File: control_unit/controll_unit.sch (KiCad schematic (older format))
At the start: 22 parts, among them J1 Screw_Terminal_1x02, J2 Screw_Terminal_1x04, P1 USB_A, P2 CONN_01X20, Q1 Q_NPN_BCE, Q2 Q_NPN_BCE, Q3 Q_NPN_BCE, U1 LM2576HV, U2 push_button, U3 push_button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

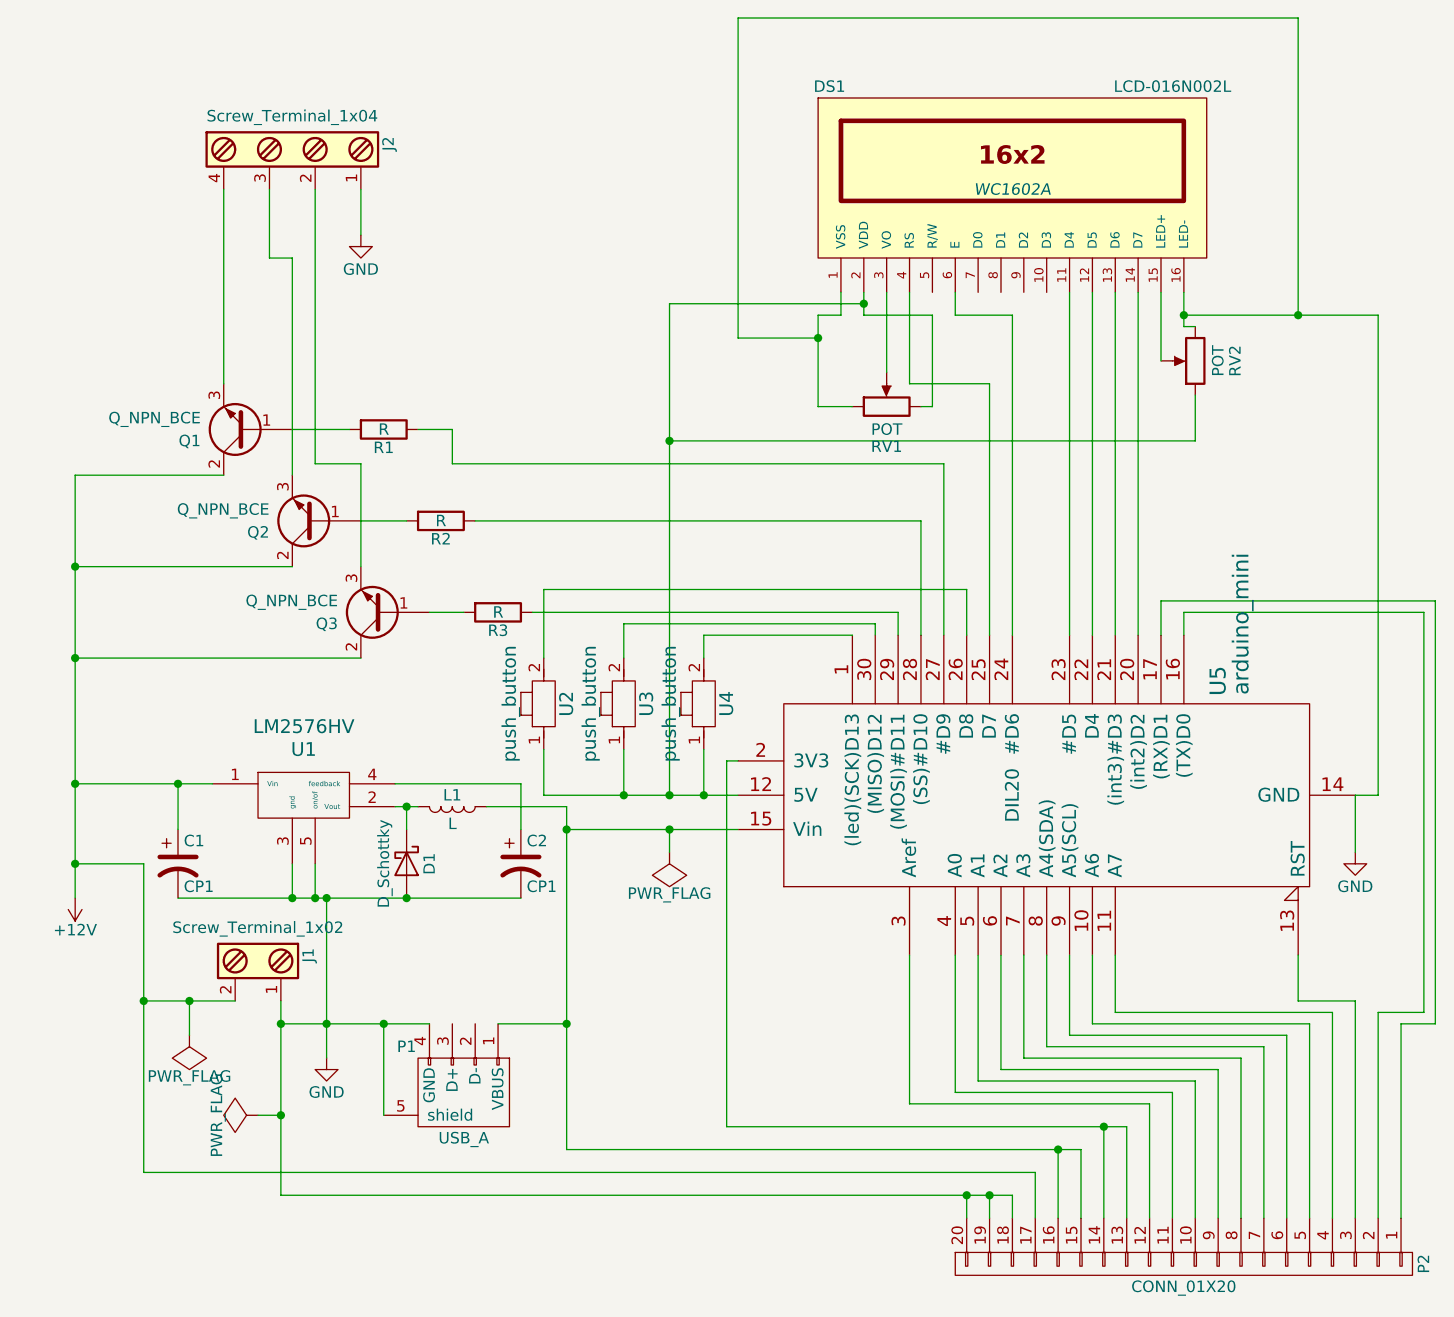
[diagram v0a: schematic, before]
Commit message: Single transistor amp pabeigs komponensu layout
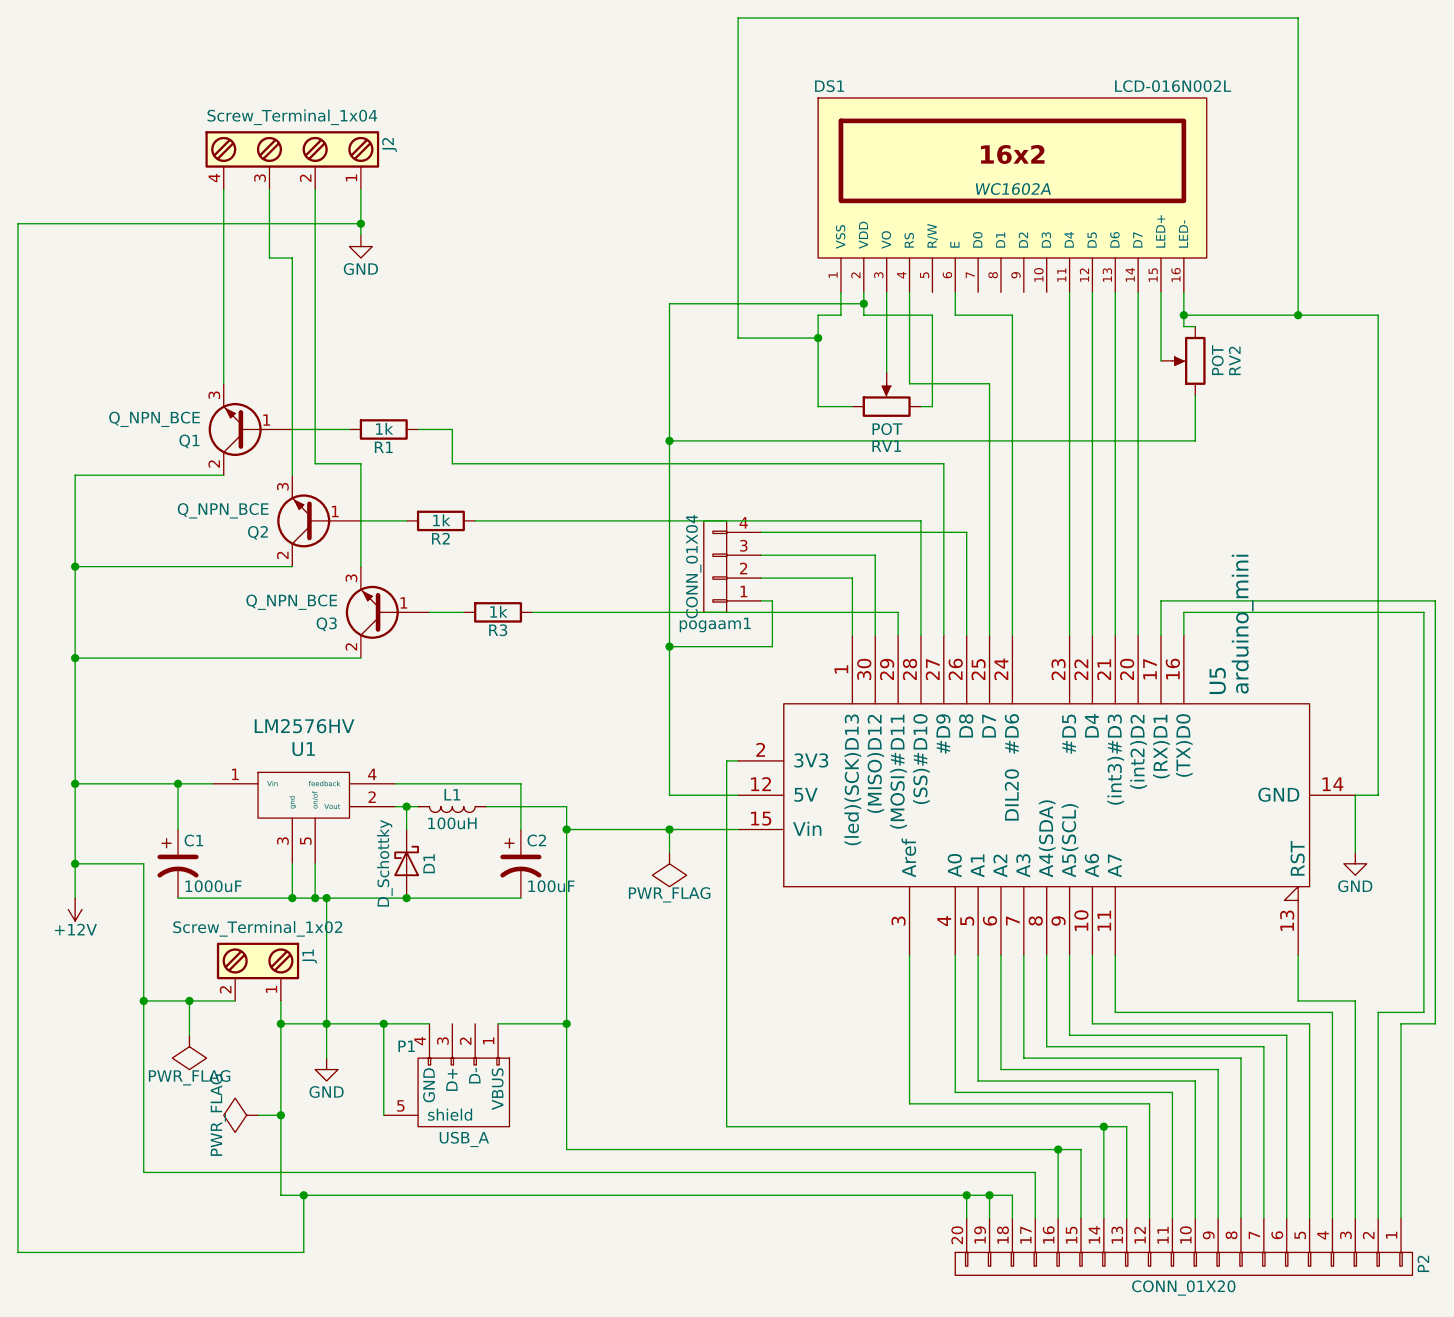
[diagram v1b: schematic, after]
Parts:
- removed U2, U3, U4: push_button, symbol push_button
- added pogaam1: CONN_01X04, Connectors:bornier4, symbol CONN_01X04
- C1: value CP1 -> 1000uF; footprint (none) -> Capacitors_THT:CP_Radial_D12.5mm_P5.00mm
- C2: value CP1 -> 100uF; footprint (none) -> Capacitors_THT:CP_Radial_D5.0mm_P2.00mm
- D1: footprint (none) -> Diodes_THT:D_DO-41_SOD81_P10.16mm_Horizontal
- J1: footprint (none) -> Connectors_Terminal_Blocks:TerminalBlock_Pheonix_PT-3.5mm_2pol
- J2: footprint (none) -> Connectors_Terminal_Blocks:TerminalBlock_Pheonix_PT-3.5mm_4pol
- L1: value L -> 100uH
- P1: footprint (none) -> Connectors:USB_A
- P2: footprint (none) -> Connectors:IDC_Header_Straight_20pins
- Q1, Q2, Q3: footprint (none) -> TO_SOT_Packages_THT:TO-220_Vertical
- R1, R2, R3: value R -> 1k; footprint (none) -> Resistors_THT:R_Axial_DIN0617_L17.0mm_D6.0mm_P25.40mm_Horizontal
- RV1, RV2: footprint (none) -> Potentiometers:Potentiometer_Trimmer_Piher_PT-10v5_Horizontal_Px5.0mm_Py5.0mm
- U1: footprint (none) -> TO_SOT_Packages_THT:TO-220-5_Pentawatt_Multiwatt-5_Vertical
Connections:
- net at DS1.2 (VDD), RV1.3, RV2.1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: now also pogaam1.1 (P1)
- net at U5.1 ((led)(SCK)D13): now also pogaam1.2 (P2)
- net at U5.26 (D8): now also pogaam1.4 (P4)
- net at U5.30 ((MISO)D12): now also pogaam1.3 (P3)
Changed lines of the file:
@@
 F 1 "LCD-016N002L" H 5850 3150 50  0000 C CNN
 F 2 "WC1602A" H 5150 2700 50  0000 C CIN
-F 3 "" H 5150 2750 50  0000 C CNN
+F 3 "https://www.openhacks.com/uploadsproductos/eone-1602a1.pdf" H 5150 2750 50  0001 C CNN
 	1    5150 2750
 	1    0    0    -1
@@
 F 1 "arduino_mini" H 5850 4400 70  0000 C CNN
 F 2 "DIL20" H 5100 5400 60  0000 C CNN
-F 3 "" H 5100 5450 60  0001 C CNN
+F 3 "https://www.arduino.cc/en/uploads/Main/ArduinoNanoManual23.pdf" H 5100 5450 60  0001 C CNN
 	1    5100 5450
 	0    -1   -1   0
@@
 F 0 "RV1" V 4425 3750 50  0000 C CNN
 F 1 "POT" V 4500 3750 50  0000 C CNN
-F 2 "" H 4600 3750 50  0000 C CNN
-F 3 "" H 4600 3750 50  0000 C CNN
+F 2 "Potentiometers:Potentiometer_Trimmer_Piher_PT-10v5_Horizontal_Px5.0mm_Py5.0mm" H 4600 3750 50  0001 C CNN
+F 3 "http://www.dipmicro.com/?datasheet=RM065.pdf" H 4600 3750 50  0001 C CNN
 	1    4600 3750
 	0    -1   -1   0
@@
 F 0 "RV2" V 5775 3550 50  0000 C CNN
 F 1 "POT" V 5850 3550 50  0000 C CNN
-F 2 "" H 5950 3550 50  0000 C CNN
-F 3 "" H 5950 3550 50  0000 C CNN
+F 2 "Potentiometers:Potentiometer_Trimmer_Piher_PT-10v5_Horizontal_Px5.0mm_Py5.0mm" H 5950 3550 50  0001 C CNN
+F 3 "http://www.dipmicro.com/?datasheet=RM065.pdf" H 5950 3550 50  0001 C CNN
 	1    5950 3550
 	-1   0    0    1
@@
 F 0 "Q3" H 2600 4700 50  0000 L CNN
 F 1 "Q_NPN_BCE" H 2600 4600 50  0000 L CNN
-F 2 "" H 2600 4750 50  0000 C CNN
-F 3 "" H 2400 4650 50  0000 C CNN
+F 2 "TO_SOT_Packages_THT:TO-220_Vertical" H 2600 4750 50  0001 C CNN
+F 3 "http://www.hobbytronics.co.uk/datasheets/TIP31.pdf" H 2400 4650 50  0001 C CNN
 	1    2400 4650
 	-1   0    0    1
@@
 F 0 "Q2" H 2300 4300 50  0000 L CNN
 F 1 "Q_NPN_BCE" H 2300 4200 50  0000 L CNN
-F 2 "" H 2300 4350 50  0000 C CNN
-F 3 "" H 2100 4250 50  0000 C CNN
+F 2 "TO_SOT_Packages_THT:TO-220_Vertical" H 2300 4350 50  0001 C CNN
+F 3 "http://www.hobbytronics.co.uk/datasheets/TIP31.pdf" H 2100 4250 50  0001 C CNN
 	1    2100 4250
 	-1   0    0    1
@@
 F 0 "Q1" H 2000 3900 50  0000 L CNN
 F 1 "Q_NPN_BCE" H 2000 3800 50  0000 L CNN
-F 2 "" H 2000 3950 50  0000 C CNN
-F 3 "" H 1800 3850 50  0000 C CNN
+F 2 "TO_SOT_Packages_THT:TO-220_Vertical" H 2000 3950 50  0001 C CNN
+F 3 "http://www.hobbytronics.co.uk/datasheets/TIP31.pdf" H 1800 3850 50  0001 C CNN
 	1    1800 3850
 	-1   0    0    1
@@
 P 2400 3850
 F 0 "R1" V 2480 3850 50  0000 C CNN
-F 1 "R" V 2400 3850 50  0000 C CNN
-F 2 "" V 2330 3850 50  0000 C CNN
-F 3 "" H 2400 3850 50  0000 C CNN
+F 1 "1k" V 2400 3850 50  0000 C CNN
+F 2 "Resistors_THT:R_Axial_DIN0617_L17.0mm_D6.0mm_P25.40mm_Horizontal" H 2330 3850 50  0001 C CNN
+F 3 "https://lib.chipdip.ru/505/DOC001505920.pdf" H 2400 3850 50  0001 C CNN
 	1    2400 3850
 	0    1    1    0
@@
 P 2650 4250
 F 0 "R2" V 2730 4250 50  0000 C CNN
-F 1 "R" V 2650 4250 50  0000 C CNN
-F 2 "" V 2580 4250 50  0000 C CNN
-F 3 "" H 2650 4250 50  0000 C CNN
+F 1 "1k" V 2650 4250 50  0000 C CNN
+F 2 "Resistors_THT:R_Axial_DIN0617_L17.0mm_D6.0mm_P25.40mm_Horizontal" H 2580 4250 50  0001 C CNN
+F 3 "https://lib.chipdip.ru/505/DOC001505920.pdf" H 2650 4250 50  0001 C CNN
 	1    2650 4250
 	0    1    1    0
@@
 P 2900 4650
 F 0 "R3" V 2980 4650 50  0000 C CNN
-F 1 "R" V 2900 4650 50  0000 C CNN
-F 2 "" V 2830 4650 50  0000 C CNN
-F 3 "" H 2900 4650 50  0000 C CNN
+F 1 "1k" V 2900 4650 50  0000 C CNN
+F 2 "Resistors_THT:R_Axial_DIN0617_L17.0mm_D6.0mm_P25.40mm_Horizontal" V 2830 4650 50  0001 C CNN
+F 3 "https://lib.chipdip.ru/505/DOC001505920.pdf" H 2900 4650 50  0001 C CNN
 	1    2900 4650
 	0    1    1    0
@@
 F 0 "J2" H 2000 3050 50  0000 C TNN
 F 1 "Screw_Terminal_1x04" V 1850 2600 50  0000 C TNN
-F 2 "" H 2000 2175 50  0001 C CNN
-F 3 "" H 1975 2800 50  0001 C CNN
+F 2 "Connectors_Terminal_Blocks:TerminalBlock_Pheonix_PT-3.5mm_4pol" H 2000 2175 50  0001 C CNN
+F 3 "http://www.altechcorp.com/PDFS/PCB-Pluggable.pdf" H 1975 2800 50  0001 C CNN
 	1    2000 2600
 	0    1    1    0
@@
 F 0 "P2" H 5900 8550 50  0000 C CNN
 F 1 "CONN_01X20" V 6000 7500 50  0000 C CNN
-F 2 "" H 5900 7500 50  0000 C CNN
-F 3 "" H 5900 7500 50  0000 C CNN
+F 2 "Connectors:IDC_Header_Straight_20pins" H 5900 7500 50  0001 C CNN
+F 3 "http://www.mmtmachrone.com/pdf/20090217224253PHa.pdf" H 5900 7500 50  0001 C CNN
 	1    5900 7500
 	0    1    1    0
@@
 F 0 "P1" H 2900 6550 50  0000 C CNN
 F 1 "USB_A" H 2650 6950 50  0000 C CNN
-F 2 "" V 2650 6650 50  0000 C CNN
-F 3 "" V 2650 6650 50  0000 C CNN
+F 2 "Connectors:USB_A" V 2650 6650 50  0001 C CNN
+F 3 "http://www.te.com/commerce/DocumentDelivery/DDEController?Action=showdoc&DocId=Data+Sheet%7F7-1773442-0%7F0306%7Fpdf%7FEnglish%7FENG_DS_7-1773442-0_0306.pdf%7F292336-1" H 2650 6650 50  0001 C CNN
 	1    2700 6750
 	-1   0    0    1
@@
 F 0 "U1" H 2050 5650 60  0000 C CNN
 F 1 "LM2576HV" H 2050 5750 60  0000 C CNN
-F 2 "" H 2100 5450 60  0001 C CNN
-F 3 "" H 2100 5450 60  0001 C CNN
+F 2 "TO_SOT_Packages_THT:TO-220-5_Pentawatt_Multiwatt-5_Vertical" H 2100 5450 60  0001 C CNN
+F 3 "http://www.ti.com/lit/ds/symlink/lm2576.pdf" H 2100 5450 60  0001 C CNN
 	1    2050 5450
 	1    0    0    -1
@@
 P 1500 5750
 F 0 "C1" H 1525 5850 50  0000 L CNN
-F 1 "CP1" H 1525 5650 50  0000 L CNN
-F 2 "" H 1500 5750 50  0000 C CNN
-F 3 "" H 1500 5750 50  0000 C CNN
+F 1 "1000uF" H 1525 5650 50  0000 L CNN
+F 2 "Capacitors_THT:CP_Radial_D12.5mm_P5.00mm" H 1500 5750 50  0001 C CNN
+F 3 "http://www.yageo.com/exep/pages/download/literatures/E-cap_2011.pdf" H 1500 5750 50  0001 C CNN
 	1    1500 5750
 	1    0    0    -1
@@
 F 0 "D1" H 2500 5850 50  0000 C CNN
 F 1 "D_Schottky" H 2500 5650 50  0000 C CNN
-F 2 "" H 2500 5750 50  0000 C CNN
-F 3 "" H 2500 5750 50  0000 C CNN
+F 2 "Diodes_THT:D_DO-41_SOD81_P10.16mm_Horizontal" H 2500 5750 50  0001 C CNN
+F 3 "https://www.pdp8online.com/mfm/board/datasheets/Fairchild_1N5820.pdf" H 2500 5750 50  0001 C CNN
 	1    2500 5750
 	0    1    1    0
@@
 P 2700 5500
 F 0 "L1" V 2650 5500 50  0000 C CNN
-F 1 "L" V 2775 5500 50  0000 C CNN
+F 1 "100uH" V 2775 5500 50  0000 C CNN
 F 2 "" H 2700 5500 50  0000 C CNN
-F 3 "" H 2700 5500 50  0000 C CNN
+F 3 "https://www.ineltro.ch/media/downloads/SAAItem/25/25670/564c7d97-85b8-461e-a4cf-90b6538cd451.pdf" H 2700 5500 50  0001 C CNN
 	1    2700 5500
 	0    1    1    0
@@
 P 3000 5750
 F 0 "C2" H 3025 5850 50  0000 L CNN
-F 1 "CP1" H 3025 5650 50  0000 L CNN
-F 2 "" H 3000 5750 50  0000 C CNN
-F 3 "" H 3000 5750 50  0000 C CNN
+F 1 "100uF" H 3025 5650 50  0000 L CNN
+F 2 "Capacitors_THT:CP_Radial_D5.0mm_P2.00mm" H 3000 5750 50  0001 C CNN
+F 3 "https://www.arduino.cc/documents/datasheets/cap100uF.pdf" H 3000 5750 50  0001 C CNN
 	1    3000 5750
 	1    0    0    -1
-$EndComp
-$Comp
-L push_button U2
-U 1 1 59121AF8
-P 3100 5050
-F 0 "U2" H 3100 4950 60  0000 C CNN
-F 1 "push_button" H 3100 5200 60  0000 C CNN
-F 2 "" H 3100 5050 60  0001 C CNN
-F 3 "" H 3100 5050 60  0001 C CNN
-	1    3100 5050
-	0    -1   -1   0
-$EndComp
-$Comp
-L push_button U3
-U 1 1 59121BAB
-P 3450 5050
-F 0 "U3" H 3450 4950 60  0000 C CNN
-F 1 "push_button" H 3450 5200 60  0000 C CNN
-F 2 "" H 3450 5050 60  0001 C CNN
-F 3 "" H 3450 5050 60  0001 C CNN
-	1    3450 5050
-	0    -1   -1   0
-$EndComp
-$Comp
-L push_button U4
-U 1 1 59121DF6
-P 3800 5050
-F 0 "U4" H 3800 4950 60  0000 C CNN
-F 1 "push_button" H 3800 5200 60  0000 C CNN
-F 2 "" H 3800 5050 60  0001 C CNN
-F 3 "" H 3800 5050 60  0001 C CNN
-	1    3800 5050
-	0    -1   -1   0
 $EndComp
 $Comp
@@
 F 0 "J1" H 1850 6400 50  0000 C TNN
 F 1 "Screw_Terminal_1x02" V 1700 6150 50  0000 C TNN
-F 2 "" H 1850 5925 50  0001 C CNN
-F 3 "" H 1825 6150 50  0001 C CNN
+F 2 "Connectors_Terminal_Blocks:TerminalBlock_Pheonix_PT-3.5mm_2pol" H 1850 5925 50  0001 C CNN
+F 3 "http://www.altechcorp.com/PDFS/PCB-Pluggable.pdf" H 1825 6150 50  0001 C CNN
 	1    1850 6150
 	0    1    1    0
@@
 	5050 3650 5050 4750
 Wire Wire Line
-	3100 5450 3950 5450
-Wire Wire Line
 	4500 3250 4500 3350
 Wire Wire Line
@@
 	3200 5600 3950 5600
 Wire Wire Line
-	4950 4750 4950 4550
-Wire Wire Line
-	4950 4550 3100 4550
-Wire Wire Line
-	3100 4550 3100 4850
-Wire Wire Line
-	4450 4750 3800 4750
-Wire Wire Line
-	3800 4750 3800 4850
-Wire Wire Line
-	4550 4750 4550 4700
-Wire Wire Line
-	4550 4700 3450 4700
-Wire Wire Line
-	3450 4700 3450 4850
-Wire Wire Line
-	3800 5250 3800 5450
-Connection ~ 3800 5450
-Wire Wire Line
-	3100 5250 3100 5450
-Wire Wire Line
-	3450 5250 3450 5450
-Connection ~ 3450 5450
+	4950 4300 4950 4750
+Wire Wire Line
+	4550 4400 4550 4750
 Connection ~ 1950 6450
 Wire Wire Line
@@
 	3650 3300 4500 3300
 Connection ~ 4500 3300
-Connection ~ 3650 5450
 Wire Wire Line
 	5950 3900 3650 3900
@@
 Wire Wire Line
 	6650 5450 6650 5700
+$Comp
+L CONN_01X04 pogaam1
+U 1 1 59132BE3
+P 3850 4450
+F 0 "pogaam1" H 3850 4700 50  0000 C CNN
+F 1 "CONN_01X04" V 3950 4450 50  0000 C CNN
+F 2 "Connectors:bornier4" H 3850 4450 50  0001 C CNN
+F 3 "http://www.mmtmachrone.com/pdf/20090217224253PHa.pdf" H 3850 4450 50  0001 C CNN
+	1    3850 4450
+	-1   0    0    1
+$EndComp
+Wire Wire Line
+	3950 5450 3650 5450
+Wire Wire Line
+	4050 4300 4950 4300
+Wire Wire Line
+	4550 4400 4050 4400
+Wire Wire Line
+	4450 4750 4450 4500
+Wire Wire Line
+	4450 4500 4050 4500
+Wire Wire Line
+	4050 4600 4100 4600
+Wire Wire Line
+	4100 4600 4100 4800
+Wire Wire Line
+	4100 4800 3650 4800
+Connection ~ 3650 4800
+Wire Wire Line
+	2300 2950 800  2950
+Wire Wire Line
+	800  2950 800  7450
+Wire Wire Line
+	800  7450 2050 7450
+Wire Wire Line
+	2050 7450 2050 7200
+Connection ~ 2050 7200
+Connection ~ 2300 2950
 $EndSCHEMATC

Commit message: Pabeigts kursa darbs Controll_unit
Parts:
- L1: footprint (none) -> Inductors_NEOSID:Neosid_Inductor_Sd75
- U5: footprint DIL20 -> arduino:arduino_mini
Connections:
- net +12V: now also J1.1, P2.3 (P3), P2.4 (P4); no longer J1.2, P2.17 (P17)
- net GND: now also DS1.10 (D3), DS1.5 (R/W), DS1.7 (D0), DS1.8 (D1), DS1.9 (D2), J1.2, J2.4, P1.2 (D-), P1.3 (D+), P2.1 (P1), P2.2 (P2); no longer J1.1, J2.1, P2.18 (P18), P2.19 (P19), P2.20 (P20)
- net at DS1.2 (VDD), RV1.3, RV2.1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: no longer pogaam1.1 (P1)
- net at U5.1 ((led)(SCK)D13): now also pogaam1.3 (P3); no longer pogaam1.2 (P2)
- net at U5.10 (A6): now also P2.18 (P18); no longer P2.5 (P5)
- net at U5.11 (A7): now also P2.19 (P19); no longer P2.4 (P4)
- net at U5.13 (RST): now also P2.20 (P20); no longer P2.3 (P3)
- net at L1.1, P1.1 (VBUS), U5.15 (Vin): now also P2.5 (P5), P2.6 (P6), pogaam1.4 (P4); no longer P2.15 (P15), P2.16 (P16)
- net at U5.16 ((TX)D0): now also P2.8 (P8); no longer P2.2 (P2)
- net at U5.17 ((RX)D1): now also P2.7 (P7); no longer P2.1 (P1)
- net at U5.26 (D8): now also pogaam1.1 (P1); no longer pogaam1.4 (P4)
- net at U5.3 (Aref): now also P2.11 (P11); no longer P2.12 (P12)
- net at U5.30 ((MISO)D12): now also pogaam1.2 (P2); no longer pogaam1.3 (P3)
- net at U5.4 (A0): now also P2.12 (P12); no longer P2.11 (P11)
- net at P2.10 (P10): now also P2.9 (P9), U5.2 (3V3); no longer U5.5 (A1)
- net at U5.6 (A2): now also P2.14 (P14); no longer P2.9 (P9)
- net at U5.7 (A3): now also P2.15 (P15); no longer P2.8 (P8)
- net at U5.8 (A4(SDA)): now also P2.16 (P16); no longer P2.7 (P7)
- net at U5.9 (A5(SCL)): now also P2.17 (P17); no longer P2.6 (P6)
- net at Q3.3 (E): now also J2.3; no longer J2.2
- net at Q2.3 (E): now also J2.2; no longer J2.3
- net at Q1.3 (E): now also J2.1; no longer J2.4
- new net: P2.13 (P13), U5.5 (A1)
